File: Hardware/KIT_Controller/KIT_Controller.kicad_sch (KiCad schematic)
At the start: 17 parts, among them SW101 TM1000, U101 Nokia_5110_LCD

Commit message: bump libs and squeeze into shape
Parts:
- added C101: EBM15DSEH, KenwoodFox:Lewis_Card_Connector, symbol KenwoodFox:EBM15DSEH
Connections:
- net GND: now also C101.15, C101.30
- new net +12V: C101.16
- new net +5V: C101.1

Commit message: Add gnd and cleanup
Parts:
- removed H103, H104, H105: MountingHole_Pad, MountingHole:MountingHole_2.5mm_Pad_TopBottom, symbol Mechanical:MountingHole_Pad
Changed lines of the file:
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@@
-    (stroke (width 0) (type default))
-  )
-  (wire (pts (xy 27.94 190.5) (xy 27.94 191.77))
     (stroke (width 0) (type default))
   )
@@
     (stroke (width 0) (type default))
   )
-  (wire (pts (xy 33.655 190.5) (xy 33.655 191.77))
-    (stroke (width 0) (type default))
-  )
   (wire (pts (xy 106.68 40.64) (xy 109.855 40.64))
     (stroke (width 0) (type default))
@@
   )
   (wire (pts (xy 226.06 76.2) (xy 226.06 76.835))
-    (stroke (width 0) (type default))
-  )
-  (wire (pts (xy 39.37 190.5) (xy 39.37 191.77))
     (stroke (width 0) (type default))
   )
@@
     )
   )
-  (symbol (lib_id "power:GND") (at 39.37 191.77 0) (unit 1)
-    (in_bom yes) (on_board yes) (dnp no)
-    (property "Reference" "#PWR0107" (at 39.37 198.12 0)
-      (effects (font (size 1.27 1.27)) hide)
-    )
-    (property "Value" "GND" (at 39.37 195.58 0)
-      (effects (font (size 1.27 1.27)))
-    )
-    (property "Footprint" "" (at 39.37 191.77 0)
-      (effects (font (size 1.27 1.27)) hide)
-    )
-    (property "Datasheet" "" (at 39.37 191.77 0)
-      (effects (font (size 1.27 1.27)) hide)
-    )
-    (pin "1")
-    (instances
-      (project "KIT_Controller"
-        (path "/d2c0d012-a149-4c33-aec9-d1ae26c850e5"
-          (reference "#PWR0107") (unit 1)
-        )
-      )
-    )
-  )
   (symbol (lib_id "power:GND") (at 16.51 191.77 0) (unit 1)
     (in_bom yes) (on_board yes) (dnp no)
@@
         (path "/d2c0d012-a149-4c33-aec9-d1ae26c850e5"
           (reference "R103") (unit 1)
-        )
-      )
-    )
-  )
-  (symbol (lib_id "Mechanical:MountingHole_Pad") (at 27.94 187.96 0) (unit 1)
-    (in_bom yes) (on_board yes) (dnp no)
-    (property "Reference" "H103" (at 25.4 183.515 0)
-      (effects (font (size 1.27 1.27)) (justify left))
-    )
-    (property "Value" "MountingHole_Pad" (at 31.115 187.9599 0)
-      (effects (font (size 1.27 1.27)) (justify left) hide)
-    )
-    (property "Footprint" "MountingHole:MountingHole_2.5mm_Pad_TopBottom" (at 27.94 187.96 0)
-      (effects (font (size 1.27 1.27)) hide)
-    )
-    (property "Datasheet" "~" (at 27.94 187.96 0)
-      (effects (font (size 1.27 1.27)) hide)
-    )
-    (pin "1")
-    (instances
-      (project "KIT_Controller"
-        (path "/d2c0d012-a149-4c33-aec9-d1ae26c850e5"
-          (reference "H103") (unit 1)
         )
       )
@@
         (path "/d2c0d012-a149-4c33-aec9-d1ae26c850e5"
           (reference "#PWR0112") (unit 1)
-        )
-      )
-    )
-  )
-  (symbol (lib_id "power:GND") (at 27.94 191.77 0) (unit 1)
-    (in_bom yes) (on_board yes) (dnp no)
-    (property "Reference" "#PWR0108" (at 27.94 198.12 0)
-      (effects (font (size 1.27 1.27)) hide)
-    )
-    (property "Value" "GND" (at 27.94 195.58 0)
-      (effects (font (size 1.27 1.27)))
-    )
-    (property "Footprint" "" (at 27.94 191.77 0)
-      (effects (font (size 1.27 1.27)) hide)
-    )
-    (property "Datasheet" "" (at 27.94 191.77 0)
-      (effects (font (size 1.27 1.27)) hide)
-    )
-    (pin "1")
-    (instances
-      (project "KIT_Controller"
-        (path "/d2c0d012-a149-4c33-aec9-d1ae26c850e5"
-          (reference "#PWR0108") (unit 1)
         )
       )
@@
     )
   )
-  (symbol (lib_id "Mechanical:MountingHole_Pad") (at 33.655 187.96 0) (unit 1)
-    (in_bom yes) (on_board yes) (dnp no)
-    (property "Reference" "H104" (at 31.115 183.515 0)
-      (effects (font (size 1.27 1.27)) (justify left))
-    )
-    (property "Value" "MountingHole_Pad" (at 36.83 187.9599 0)
-      (effects (font (size 1.27 1.27)) (justify left) hide)
-    )
-    (property "Footprint" "MountingHole:MountingHole_2.5mm_Pad_TopBottom" (at 33.655 187.96 0)
-      (effects (font (size 1.27 1.27)) hide)
-    )
-    (property "Datasheet" "~" (at 33.655 187.96 0)
-      (effects (font (size 1.27 1.27)) hide)
-    )
-    (pin "1")
-    (instances
-      (project "KIT_Controller"
-        (path "/d2c0d012-a149-4c33-aec9-d1ae26c850e5"
-          (reference "H104") (unit 1)
-        )
-      )
-    )
-  )
   (symbol (lib_id "power:+3V3") (at 272.415 76.835 0) (unit 1)
     (in_bom yes) (on_board yes) (dnp no) (fields_autoplaced)
@@
     )
   )
-  (symbol (lib_id "KenwoodFox:KITSUNE_LOGO") (at 190.5 173.355 0) (unit 1)
-    (in_bom yes) (on_board yes) (dnp no) (fields_autoplaced)
-    (property "Reference" "#L101" (at 190.5 169.0634 0)
-      (effects (font (size 1.27 1.27)) hide)
-    )
-    (property "Value" "KITSUNE_LOGO" (at 190.5 179.705 0)
-      (effects (font (size 1.27 1.27)) hide)
-    )
-    (property "Footprint" "" (at 190.5 173.355 0)
-      (effects (font (size 1.27 1.27)) hide)
-    )
-    (property "Datasheet" "" (at 190.5 173.355 0)
-      (effects (font (size 1.27 1.27)) hide)
-    )
-    (instances
-      (project "KIT_Controller"
-        (path "/d2c0d012-a149-4c33-aec9-d1ae26c850e5"
-          (reference "#L101") (unit 1)
-        )
-      )
-    )
-  )
   (symbol (lib_id "KenwoodFox:TM1000") (at 167.64 89.535 0) (unit 1)
     (in_bom yes) (on_board yes) (dnp no) (fields_autoplaced)
@@
     )
   )
-  (symbol (lib_id "power:GND") (at 33.655 191.77 0) (unit 1)
-    (in_bom yes) (on_board yes) (dnp no)
-    (property "Reference" "#PWR0106" (at 33.655 198.12 0)
-      (effects (font (size 1.27 1.27)) hide)
-    )
-    (property "Value" "GND" (at 33.655 195.58 0)
-      (effects (font (size 1.27 1.27)))
-    )
-    (property "Footprint" "" (at 33.655 191.77 0)
-      (effects (font (size 1.27 1.27)) hide)
-    )
-    (property "Datasheet" "" (at 33.655 191.77 0)
-      (effects (font (size 1.27 1.27)) hide)
-    )
-    (pin "1")
-    (instances
-      (project "KIT_Controller"
-        (path "/d2c0d012-a149-4c33-aec9-d1ae26c850e5"
-          (reference "#PWR0106") (unit 1)
-        )
-      )
-    )
-  )
   (symbol (lib_id "Device:R_Small") (at 247.65 92.71 180) (unit 1)
     (in_bom yes) (on_board yes) (dnp no)
@@
         )
       )
-    )
-  )
-  (symbol (lib_id "Mechanical:MountingHole_Pad") (at 39.37 187.96 0) (unit 1)
-    (in_bom yes) (on_board yes) (dnp no)
-    (property "Reference" "H105" (at 36.83 183.515 0)
-      (effects (font (size 1.27 1.27)) (justify left))
-    )
-    (property "Value" "MountingHole_Pad" (at 42.545 187.9599 0)
-      (effects (font (size 1.27 1.27)) (justify left) hide)
-    )
-    (property "Footprint" "MountingHole:MountingHole_2.5mm_Pad_TopBottom" (at 39.37 187.96 0)
-      (effects (font (size 1.27 1.27)) hide)
-    )
-    (property "Datasheet" "~" (at 39.37 187.96 0)
-      (effects (font (size 1.27 1.27)) hide)
-    )
-    (pin "1")
-    (instances
-      (project "KIT_Controller"
-        (path "/d2c0d012-a149-4c33-aec9-d1ae26c850e5"
-          (reference "H105") (unit 1)
-        )
-      )

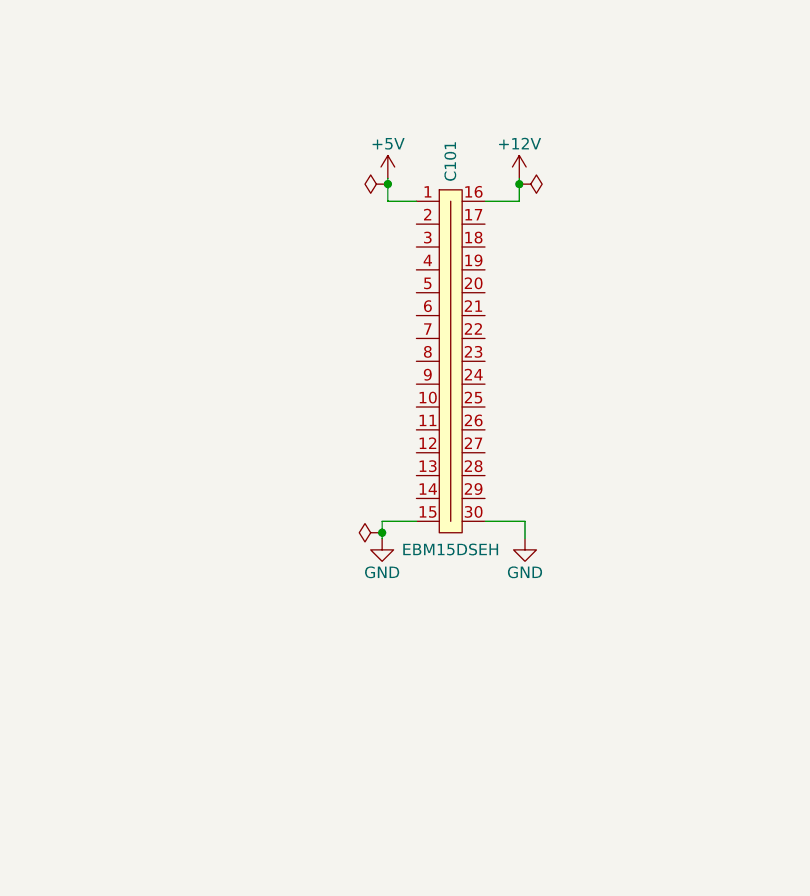
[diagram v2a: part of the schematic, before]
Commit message: include upstream fixes in kit controller
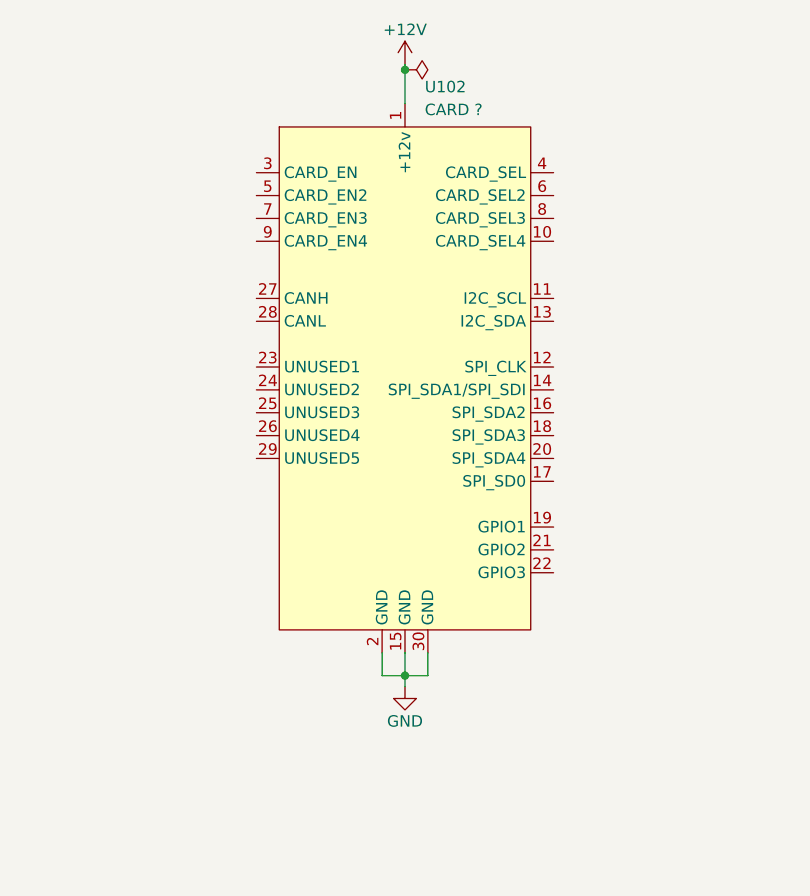
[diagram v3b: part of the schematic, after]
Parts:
- removed C101: EBM15DSEH, KenwoodFox:Lewis_Card_Connector, symbol KenwoodFox:EBM15DSEH
- added U102: CARD ?, KenwoodFox:Lewis_Card_Connector, symbol KenwoodFox:KIT_CONNECTOR
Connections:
- net +12V: now also U102.1 (+12v)
- net GND: now also U102.15 (GND), U102.2 (GND), U102.30 (GND)

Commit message: Bump to new ver
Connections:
- no-connect marks 10 -> 8
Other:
- removed sheet Short Range Modem
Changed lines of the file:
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@@
   (no_connect (at 212.09 97.155))
   (no_connect (at 53.34 46.99))
-  (no_connect (at 53.34 54.61))
   (no_connect (at 212.09 92.075))
   (no_connect (at 212.09 94.615))
   (no_connect (at 212.09 88.265))
-  (no_connect (at 53.34 52.705))
   (no_connect (at 212.09 99.695))
   (no_connect (at 53.34 45.085))
@@
     (stroke (width 0) (type default))
   )
-  (wire (pts (xy 47.625 54.61) (xy 53.34 54.61))
+  (wire (pts (xy 47.625 55.245) (xy 53.34 55.245))
     (stroke (width 0) (type default))
   )
@@
   (wire (pts (xy 264.795 97.155) (xy 272.415 97.155))
     (stroke (width 0) (type default))
+  )
+  (label "SDA" (at 53.34 52.705 180) (fields_autoplaced)
+    (effects (font (size 1.27 1.27)) (justify right bottom))
+  )
+  (label "SCL" (at 53.34 55.245 180) (fields_autoplaced)
+    (effects (font (size 1.27 1.27)) (justify right bottom))
   )
   (symbol (lib_id "Device:LED") (at 272.415 84.455 270) (unit 1)
@@
       (effects (font (size 1.27 1.27)) (justify right))
     )
-    (pin "SCL" output (at 47.625 54.61 0)
+    (pin "SCL" output (at 47.625 55.245 0)
       (effects (font (size 1.27 1.27)) (justify right))
     )
@@
       )
     )
-  )
-  (sheet (at 26.67 93.345) (size 21.59 21.59) (fields_autoplaced)
-    (stroke (width 0.1524) (type solid))
-    (fill (color 0 0 0 0.0000))
-    (property "Sheetname" "Short Range Modem" (at 26.67 92.6334 0)
-      (effects (font (size 1.27 1.27)) (justify left bottom))
-    )
-    (property "Sheetfile" "ShortRangeModem.kicad_sch" (at 26.67 115.5196 0)
-      (effects (font (size 1.27 1.27)) (justify left top))
-    )
-    (instances
-      (project "KIT_Controller"
-        (path "/d2c0d012-a149-4c33-aec9-d1ae26c850e5" (page "3"))
-      )
-    )
